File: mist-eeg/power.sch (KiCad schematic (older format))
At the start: 22 parts, among them J1 Power_5V-14V, Q1 NMOS_DGS (3V3), U1 LTC2947

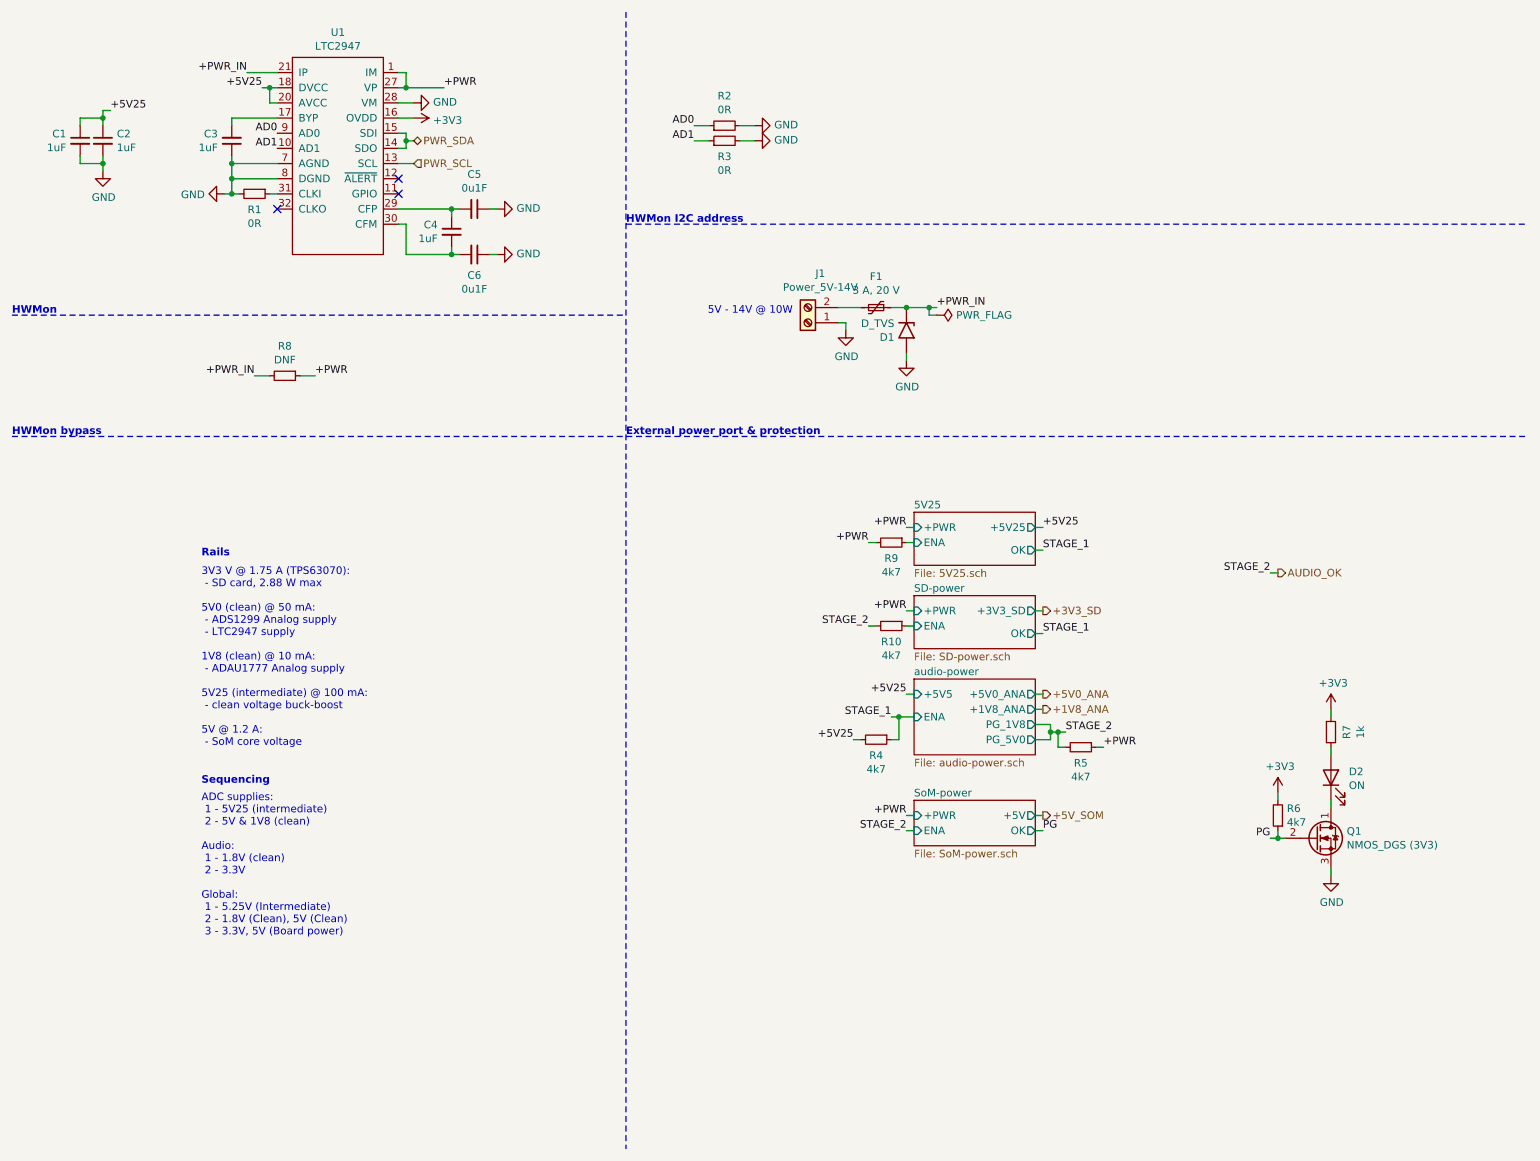
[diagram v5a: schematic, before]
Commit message: Change buckboost regulator used
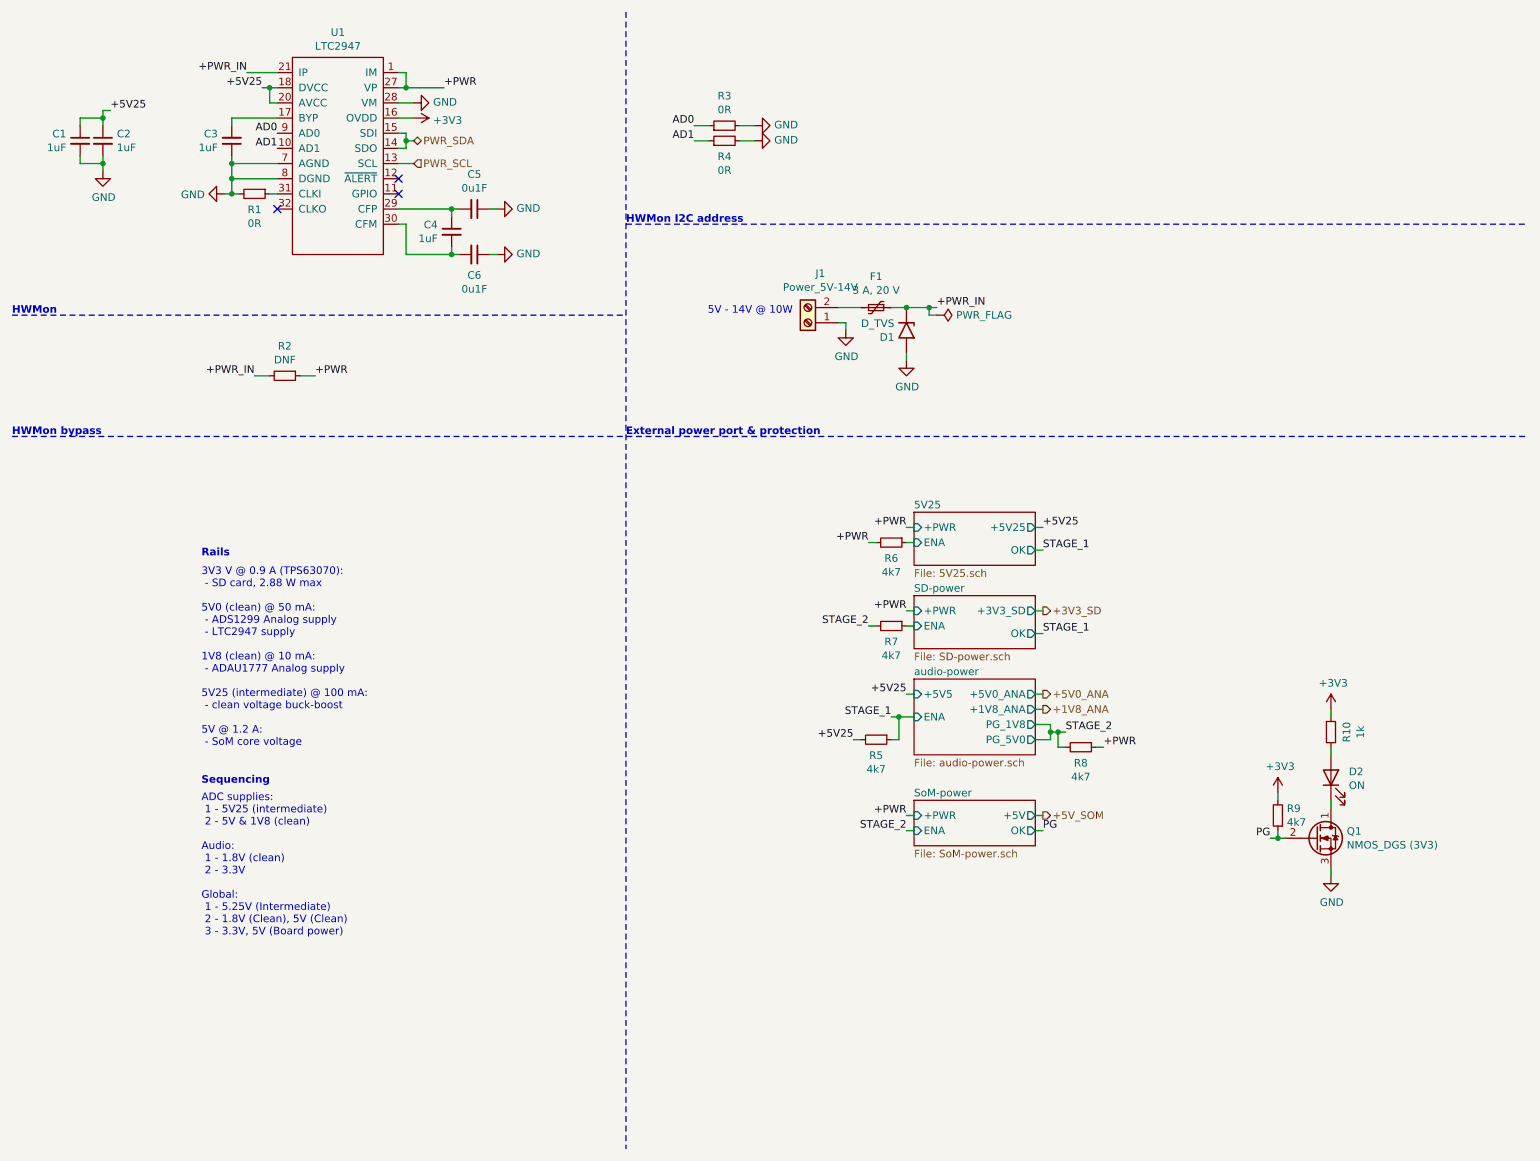
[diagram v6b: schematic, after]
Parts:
- renumbered R7 to R10, R8 to R2, R2 to R3, R3 to R4, R4 to R5, R9 to R6, R10 to R7, R5 to R8, R6 to R9
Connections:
- net AUDIO_OK renamed STAGE_2
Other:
- note added: "3V3 V @ 0.9 A (TPS63070):\n - SD card, 2.88 W max\n\n5V0 (clean) @ 50 mA:\n - ADS1299 Analog supply\n - LTC2947 supply\n\n1V8 (clean) @ 10 mA:\n - ADAU1777 Analog supply\n\n5V25 (intermediate) @ 100 mA:\n - clean voltage buck-boost\n\n5V @ 1.2 A:\n - SoM core voltage"
- note removed: "3V3 V @ 1.75 A (TPS63070):\n - SD card, 2.88 W max\n\n5V0 (clean) @ 50 mA:\n - ADS1299 Analog supply\n - LTC2947 supply\n\n1V8 (clean) @ 10 mA:\n - ADAU1777 Analog supply\n\n5V25 (intermediate) @ 100 mA:\n - clean voltage buck-boost\n\n5V @ 1.2 A:\n - SoM core voltage"

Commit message: Switch to POL switching regulator to accelerate production of the board
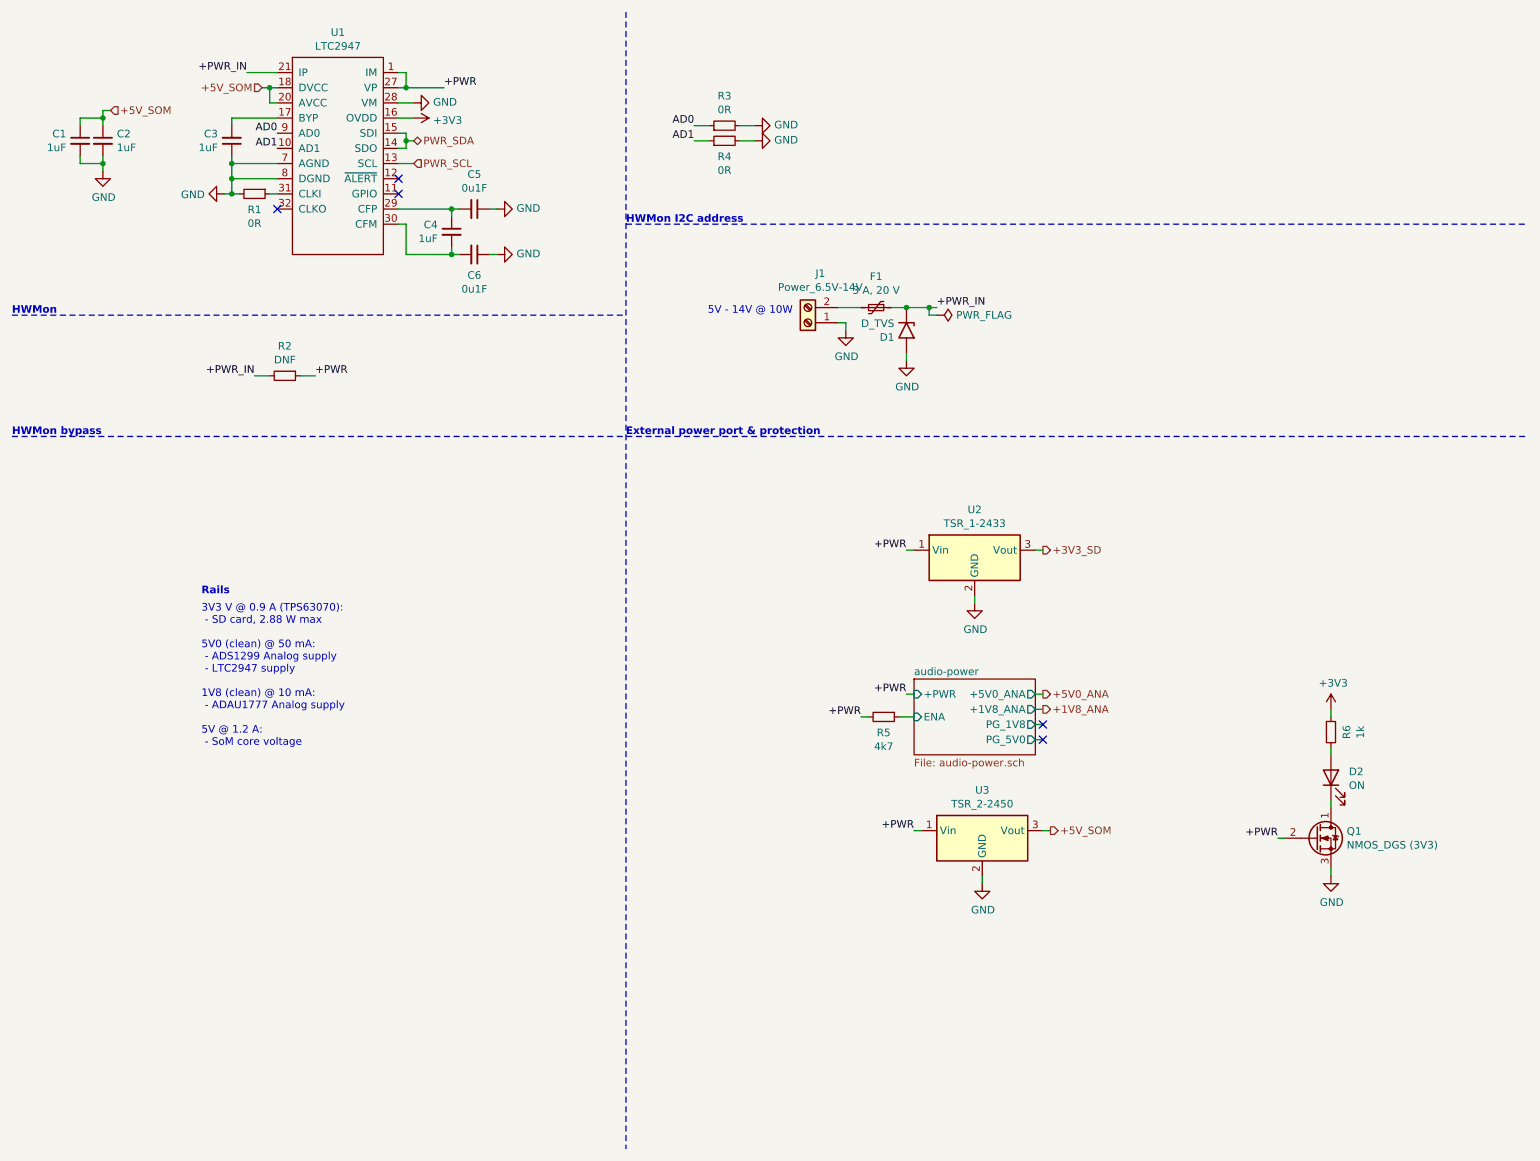
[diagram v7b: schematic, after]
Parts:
- removed R6, R7, R8, R9: 4k7, Resistor_SMD:R_0201_0603Metric, symbol Device:R_Small
- added U2: TSR_1-2433, Converter_DCDC:Converter_DCDC_TRACO_TSR-1_THT, symbol Regulator_Switching:TSR_1-2433
- added U3: TSR_2-2450, Converter_DCDC:Converter_DCDC_TRACO_TSR-1_THT, symbol Regulator_Switching:TSR_1-2450
- J1: value Power_5V-14V -> Power_6.5V-14V
- renumbered R10 to R6
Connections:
- net PG is gone; now on net +PWR: Q1.2 (G)
- net +3V3_SD: now also U2.3 (Vout)
- net +5V_SOM: now also C1.1, C2.1, U1.18 (DVCC), U1.20 (AVCC), U3.3 (Vout)
- net +PWR: now also R5.2, U2.1 (Vin), U3.1 (Vin)
- net GND: now also U2.2 (GND), U3.2 (GND)
- removed net +5V25: C1.1, C2.1, R5.2, U1.18 (DVCC), U1.20 (AVCC)
- net STAGE_1 renamed audio-power/ENA
- no-connect marks 3 -> 5
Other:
- note added: "3V3 V @ 0.9 A (TPS63070):\n - SD card, 2.88 W max\n\n5V0 (clean) @ 50 mA:\n - ADS1299 Analog supply\n - LTC2947 supply\n\n1V8 (clean) @ 10 mA:\n - ADAU1777 Analog supply\n\n5V @ 1.2 A:\n - SoM core voltage"
- note removed: "3V3 V @ 0.9 A (TPS63070):\n - SD card, 2.88 W max\n\n5V0 (clean) @ 50 mA:\n - ADS1299 Analog supply\n - LTC2947 supply\n\n1V8 (clean) @ 10 mA:\n - ADAU1777 Analog supply\n\n5V25 (intermediate) @ 100 mA:\n - clean voltage buck-boost\n\n5V @ 1.2 A:\n - SoM core voltage"
- note removed: "ADC supplies:\n 1 - 5V25 (intermediate)\n 2 - 5V & 1V8 (clean)\n\nAudio:\n 1 - 1.8V (clean)\n 2 - 3.3V\n\nGlobal:\n 1 - 5.25V (Intermediate)\n 2 - 1.8V (Clean), 5V (Clean)\n 3 - 3.3V, 5V (Board power)"
- note removed: "Sequencing"
- moved on the sheet: R5
